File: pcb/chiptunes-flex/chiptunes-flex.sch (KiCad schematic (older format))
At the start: 6 parts, among them U1 ATtiny4-TS

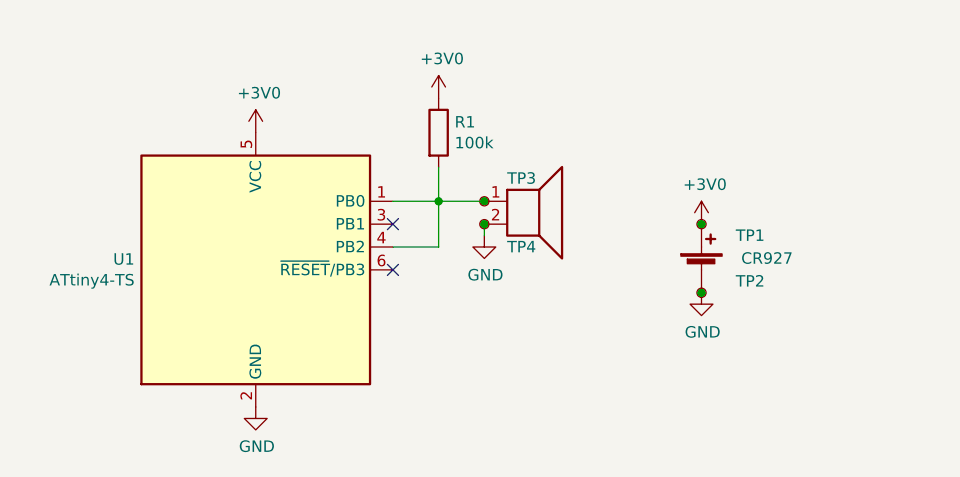
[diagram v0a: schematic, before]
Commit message: pcb: add low pass filter
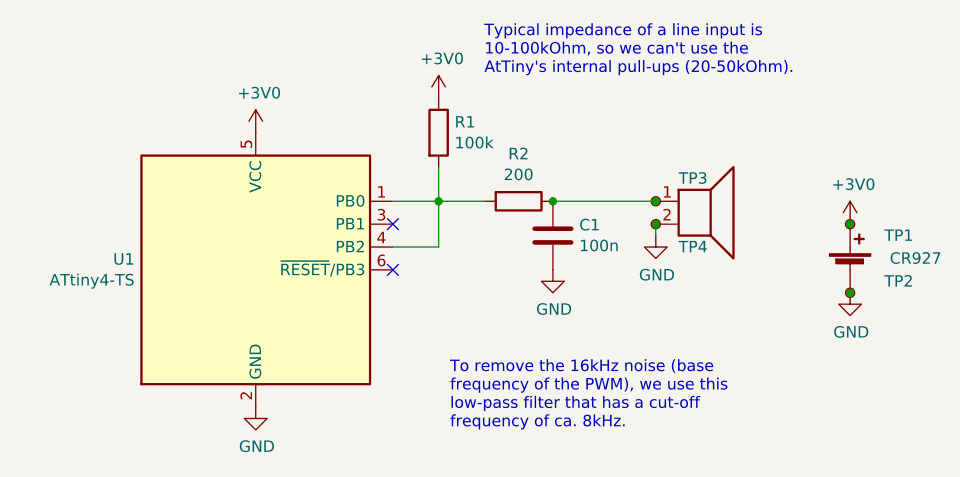
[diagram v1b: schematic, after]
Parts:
- added C1: 100n, Capacitor_SMD:C_0805_2012Metric, symbol Device:C
- added R2: 200, Resistor_SMD:R_0805_2012Metric, symbol Device:R
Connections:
- net GND: now also C1.2
- net at R1.2, U1.1 (PB0), U1.4 (PB2): now also R2.2; no longer TP3.1
- new net: C1.1, R2.1, TP3.1
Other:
- note added: "To remove the 16kHz noise (base \nfrequency of the PWM), we use this \nlow-pass filter that has a cut-off \nfrequency of ca. 8kHz."
- note added: "Typical impedance of a line input is \n10-100kOhm, so we can't use the \nAtTiny's internal pull-ups (20-50kOhm)."
- moved on the sheet: TP1, TP2, TP3, TP4
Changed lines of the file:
@@
 L Device:Battery_Cell #BT1
 U 1 1 5F1956B2
-P 6800 3600
-F 0 "#BT1" H 6683 3696 50  0001 R CNN
-F 1 "CR927" H 7200 3650 50  0000 R CNN
-F 2 "" V 6800 3660 50  0001 C CNN
-F 3 "~" V 6800 3660 50  0001 C CNN
-	1    6800 3600
+P 7450 3600
+F 0 "#BT1" H 7333 3696 50  0001 R CNN
+F 1 "CR927" H 7850 3650 50  0000 R CNN
+F 2 "" V 7450 3660 50  0001 C CNN
+F 3 "~" V 7450 3660 50  0001 C CNN
+	1    7450 3600
 	1    0    0    -1
 $EndComp
 $Comp
-L power:GND #PWR?
+L power:GND #PWR0101
 U 1 1 5F1959C5
-P 6800 3700
-F 0 "#PWR?" H 6800 3450 50  0001 C CNN
-F 1 "GND" H 6805 3527 50  0000 C CNN
-F 2 "" H 6800 3700 50  0001 C CNN
-F 3 "" H 6800 3700 50  0001 C CNN
-	1    6800 3700
+P 7450 3700
+F 0 "#PWR0101" H 7450 3450 50  0001 C CNN
+F 1 "GND" H 7455 3527 50  0000 C CNN
+F 2 "" H 7450 3700 50  0001 C CNN
+F 3 "" H 7450 3700 50  0001 C CNN
+	1    7450 3700
 	1    0    0    -1
 $EndComp
 $Comp
-L power:+3V0 #PWR?
+L power:+3V0 #PWR0102
 U 1 1 5F195F35
-P 6800 3400
-F 0 "#PWR?" H 6800 3250 50  0001 C CNN
-F 1 "+3V0" H 6815 3573 50  0000 C CNN
-F 2 "" H 6800 3400 50  0001 C CNN
-F 3 "" H 6800 3400 50  0001 C CNN
-	1    6800 3400
+P 7450 3400
+F 0 "#PWR0102" H 7450 3250 50  0001 C CNN
+F 1 "+3V0" H 7465 3573 50  0000 C CNN
+F 2 "" H 7450 3400 50  0001 C CNN
+F 3 "" H 7450 3400 50  0001 C CNN
+	1    7450 3400
 	1    0    0    -1
 $EndComp
 $Comp
-L power:+3V0 #PWR?
+L power:+3V0 #PWR0103
 U 1 1 5F196204
 P 4850 3000
-F 0 "#PWR?" H 4850 2850 50  0001 C CNN
+F 0 "#PWR0103" H 4850 2850 50  0001 C CNN
 F 1 "+3V0" H 4865 3173 50  0000 C CNN
 F 2 "" H 4850 3000 50  0001 C CNN
@@
 $EndComp
 $Comp
-L power:GND #PWR?
+L power:GND #PWR0104
 U 1 1 5F196445
 P 4850 4200
-F 0 "#PWR?" H 4850 3950 50  0001 C CNN
+F 0 "#PWR0104" H 4850 3950 50  0001 C CNN
 F 1 "GND" H 4855 4027 50  0000 C CNN
 F 2 "" H 4850 4200 50  0001 C CNN
@@
 L Device:Speaker #LS1
 U 1 1 5F196D45
-P 6050 3300
-F 0 "#LS1" H 6013 3617 50  0001 C CNN
-F 1 "Speaker" H 6013 3525 50  0001 C CNN
-F 2 "" H 6050 3100 50  0001 C CNN
-F 3 "~" H 6040 3250 50  0001 C CNN
-	1    6050 3300
+P 6800 3300
+F 0 "#LS1" H 6763 3617 50  0001 C CNN
+F 1 "Speaker" H 6763 3525 50  0001 C CNN
+F 2 "" H 6800 3100 50  0001 C CNN
+F 3 "~" H 6790 3250 50  0001 C CNN
+	1    6800 3300
 	1    0    0    -1
 $EndComp
@@
 Connection ~ 5650 3300
 Wire Wire Line
-	5650 3300 5850 3300
-Wire Wire Line
 	5650 3300 5650 3150
 $Comp
-L power:GND #PWR?
+L power:GND #PWR0105
 U 1 1 5F1981AF
-P 5850 3450
-F 0 "#PWR?" H 5850 3200 50  0001 C CNN
-F 1 "GND" H 5855 3277 50  0000 C CNN
-F 2 "" H 5850 3450 50  0001 C CNN
-F 3 "" H 5850 3450 50  0001 C CNN
-	1    5850 3450
+P 6600 3450
+F 0 "#PWR0105" H 6600 3200 50  0001 C CNN
+F 1 "GND" H 6605 3277 50  0000 C CNN
+F 2 "" H 6600 3450 50  0001 C CNN
+F 3 "" H 6600 3450 50  0001 C CNN
+	1    6600 3450
 	1    0    0    -1
 $EndComp
 $Comp
-L power:+3V0 #PWR?
+L power:+3V0 #PWR0106
 U 1 1 5F198416
 P 5650 2850
-F 0 "#PWR?" H 5650 2700 50  0001 C CNN
+F 0 "#PWR0106" H 5650 2700 50  0001 C CNN
 F 1 "+3V0" H 5665 3023 50  0000 C CNN
 F 2 "" H 5650 2850 50  0001 C CNN
@@
 NoConn ~ 5450 3600
 Wire Wire Line
-	5850 3450 5850 3400
+	6600 3450 6600 3400
 $Comp
 L Connector:TestPoint_Small TP3
 U 1 1 5F19A878
-P 5850 3300
-F 0 "TP3" H 5950 3400 50  0000 L CNN
-F 1 "audio+" H 6200 3300 50  0001 L CNN
-F 2 "TestPoint:TestPoint_Pad_D2.0mm" H 6050 3300 50  0001 C CNN
-F 3 "~" H 6050 3300 50  0001 C CNN
-	1    5850 3300
+P 6600 3300
+F 0 "TP3" H 6700 3400 50  0000 L CNN
+F 1 "audio+" H 6950 3300 50  0001 L CNN
+F 2 "TestPoint:TestPoint_Pad_D2.0mm" H 6800 3300 50  0001 C CNN
+F 3 "~" H 6800 3300 50  0001 C CNN
+	1    6600 3300
 	1    0    0    -1
 $EndComp
-Connection ~ 5850 3300
+Connection ~ 6600 3300
 $Comp
 L Connector:TestPoint_Small TP4
 U 1 1 5F19AD90
-P 5850 3400
-F 0 "TP4" H 5950 3300 50  0000 L CNN
-F 1 "audio-" H 6200 3400 50  0001 L CNN
-F 2 "TestPoint:TestPoint_Pad_D2.0mm" H 6050 3400 50  0001 C CNN
-F 3 "~" H 6050 3400 50  0001 C CNN
-	1    5850 3400
+P 6600 3400
+F 0 "TP4" H 6700 3300 50  0000 L CNN
+F 1 "audio-" H 6950 3400 50  0001 L CNN
+F 2 "TestPoint:TestPoint_Pad_D2.0mm" H 6800 3400 50  0001 C CNN
+F 3 "~" H 6800 3400 50  0001 C CNN
+	1    6600 3400
 	1    0    0    -1
 $EndComp
-Connection ~ 5850 3400
+Connection ~ 6600 3400
 $Comp
 L Connector:TestPoint_Small TP1
 U 1 1 5F19AF7A
-P 6800 3400
-F 0 "TP1" H 6950 3350 50  0000 L CNN
-F 1 "bat+" H 6848 3355 50  0001 L CNN
-F 2 "TestPoint:TestPoint_Pad_D2.0mm" H 7000 3400 50  0001 C CNN
-F 3 "~" H 7000 3400 50  0001 C CNN
-	1    6800 3400
+P 7450 3400
+F 0 "TP1" H 7600 3350 50  0000 L CNN
+F 1 "bat+" H 7498 3355 50  0001 L CNN
+F 2 "TestPoint:TestPoint_Pad_D2.0mm" H 7650 3400 50  0001 C CNN
+F 3 "~" H 7650 3400 50  0001 C CNN
+	1    7450 3400
 	1    0    0    -1
 $EndComp
-Connection ~ 6800 3400
+Connection ~ 7450 3400
 $Comp
 L Connector:TestPoint_Small TP2
 U 1 1 5F19B282
-P 6800 3700
-F 0 "TP2" H 6950 3750 50  0000 L CNN
-F 1 "bat-" H 6848 3655 50  0001 L CNN
-F 2 "TestPoint:TestPoint_Pad_D2.0mm" H 7000 3700 50  0001 C CNN
-F 3 "~" H 7000 3700 50  0001 C CNN
-	1    6800 3700
+P 7450 3700
+F 0 "TP2" H 7600 3750 50  0000 L CNN
+F 1 "bat-" H 7498 3655 50  0001 L CNN
+F 2 "TestPoint:TestPoint_Pad_D2.0mm" H 7650 3700 50  0001 C CNN
+F 3 "~" H 7650 3700 50  0001 C CNN
+	1    7450 3700
 	1    0    0    -1
 $EndComp
-Connection ~ 6800 3700
+Connection ~ 7450 3700
+$Comp
+L Device:R R2
+U 1 1 5F1D9E27
+P 6000 3300
+F 0 "R2" V 5793 3300 50  0000 C CNN
+F 1 "200" V 5884 3300 50  0000 C CNN
+F 2 "Resistor_SMD:R_0805_2012Metric" V 5930 3300 50  0001 C CNN
+F 3 "~" H 6000 3300 50  0001 C CNN
+	1    6000 3300
+	0    1    1    0
+$EndComp
+$Comp
+L Device:C C1
+U 1 1 5F1DA44F
+P 6150 3450
+F 0 "C1" H 6265 3496 50  0000 L CNN
+F 1 "100n" H 6265 3405 50  0000 L CNN
+F 2 "Capacitor_SMD:C_0805_2012Metric" H 6188 3300 50  0001 C CNN
+F 3 "~" H 6150 3450 50  0001 C CNN
+	1    6150 3450
+	1    0    0    -1
+$EndComp
+Wire Wire Line
+	5650 3300 5850 3300
+Wire Wire Line
+	6150 3300 6600 3300
+Connection ~ 6150 3300
+$Comp
+L power:GND #PWR0107
+U 1 1 5F1E259E
+P 6150 3600
+F 0 "#PWR0107" H 6150 3350 50  0001 C CNN
+F 1 "GND" H 6155 3427 50  0000 C CNN
+F 2 "" H 6150 3600 50  0001 C CNN
+F 3 "" H 6150 3600 50  0001 C CNN
+	1    6150 3600
+	1    0    0    -1
+$EndComp
+Text Notes 5700 4300 0    50   ~ 0
+To remove the 16kHz noise (base \nfrequency of the PWM), we use this \nlow-pass filter that has a cut-off \nfrequency of ca. 8kHz.
+Text Notes 5850 2750 0    50   ~ 0
+Typical impedance of a line input is \n10-100kOhm, so we can't use the \nAtTiny's internal pull-ups (20-50kOhm).
 $EndSCHEMATC
